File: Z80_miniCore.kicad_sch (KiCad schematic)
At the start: 40 parts, among them J1 ICSP, J2 UART, J3 I2C, J5 MicroSD, J7 USB_B_Mini, SW1 ON|OFF, SW2 Z80_RESET, SW3 CUSTOM, U1 Z84C00/PLCC, U2 PIC1-MMU, U3 28C256, U4 74HC138, U7 IS62C256AL, Y1 CANNED-DIP8, Y2 Crystal

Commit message: finish routing.
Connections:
- net GND: now also U4.5 (~{E1})
- net RFSH: no longer U4.5 (~{E1})
- no-connect marks 13 -> 14
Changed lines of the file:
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@@
+	)
+	(junction
+		(at 60.96 142.24)
+		(diameter 0)
+		(color 0 0 0 0)
 	)
 	(junction
@@
 	)
 	(no_connect
+		(at 22.86 41.91)
+	)
+	(no_connect
 		(at 245.11 115.57)
 	)
@@
 	(wire
 		(pts
+			(xy 60.96 142.24) (xy 60.96 149.86)
+		)
+		(stroke
+			(width 0)
+			(type default)
+		)
+	)
+	(wire
+		(pts
 			(xy 224.79 110.49) (xy 224.79 116.84)
 		)
@@
 	(wire
 		(pts
-			(xy 63.5 142.24) (xy 69.85 142.24)
+			(xy 60.96 142.24) (xy 69.85 142.24)
 		)
 		(stroke
@@
 	(wire
 		(pts
-			(xy 60.96 132.08) (xy 60.96 149.86)
+			(xy 60.96 132.08) (xy 60.96 142.24)
 		)
 		(stroke
@@
 		(effects
 			(font
-				(size 1.27 1.27)
-			)
-			(justify left bottom)
-		)
-	)
-	(label "RFSH"
-		(at 63.5 142.24 0)
-		(effects
-			(font

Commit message: Replace 8x10K_R w/ 1xRN8. Refine footprints.
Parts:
- removed R10, R11, R12, R4, R5, R6, R7, R9: 10K, Resistor_THT:R_Axial_DIN0207_L6.3mm_D2.5mm_P10.16mm_Horizontal, symbol Device:R
- added RN1: R_Network08, Resistor_THT:R_Array_SIP9, symbol Device:R_Network08
- C8: footprint Capacitor_THT:C_Disc_D3.4mm_W2.1mm_P2.50mm -> Capacitor_THT:C_Radial_D4.0mm_H5.0mm_P1.50mm
- C9: value 100uF -> 10uF
- J5: footprint Connector_PinSocket_2.54mm:PinSocket_1x06_P2.54mm_Vertical -> Connector_PinHeader_2.54mm:PinHeader_1x06_P2.54mm_Vertical
- R13: value 4k7 -> 10K
- R14: value 330 -> 10K
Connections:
- net BUSREQ: now also RN1.8 (R7)
- net INT: now also RN1.9 (R8)
- net IORQ: now also RN1.3 (R2)
- net MREQ: now also RN1.2 (R1)
- net NMI: now also RN1.7 (R6)
- net RD: now also RN1.4 (R3)
- net VCC: now also RN1.1 (common)
- net WAIT: now also RN1.6 (R5)
- net WR: now also RN1.5 (R4)

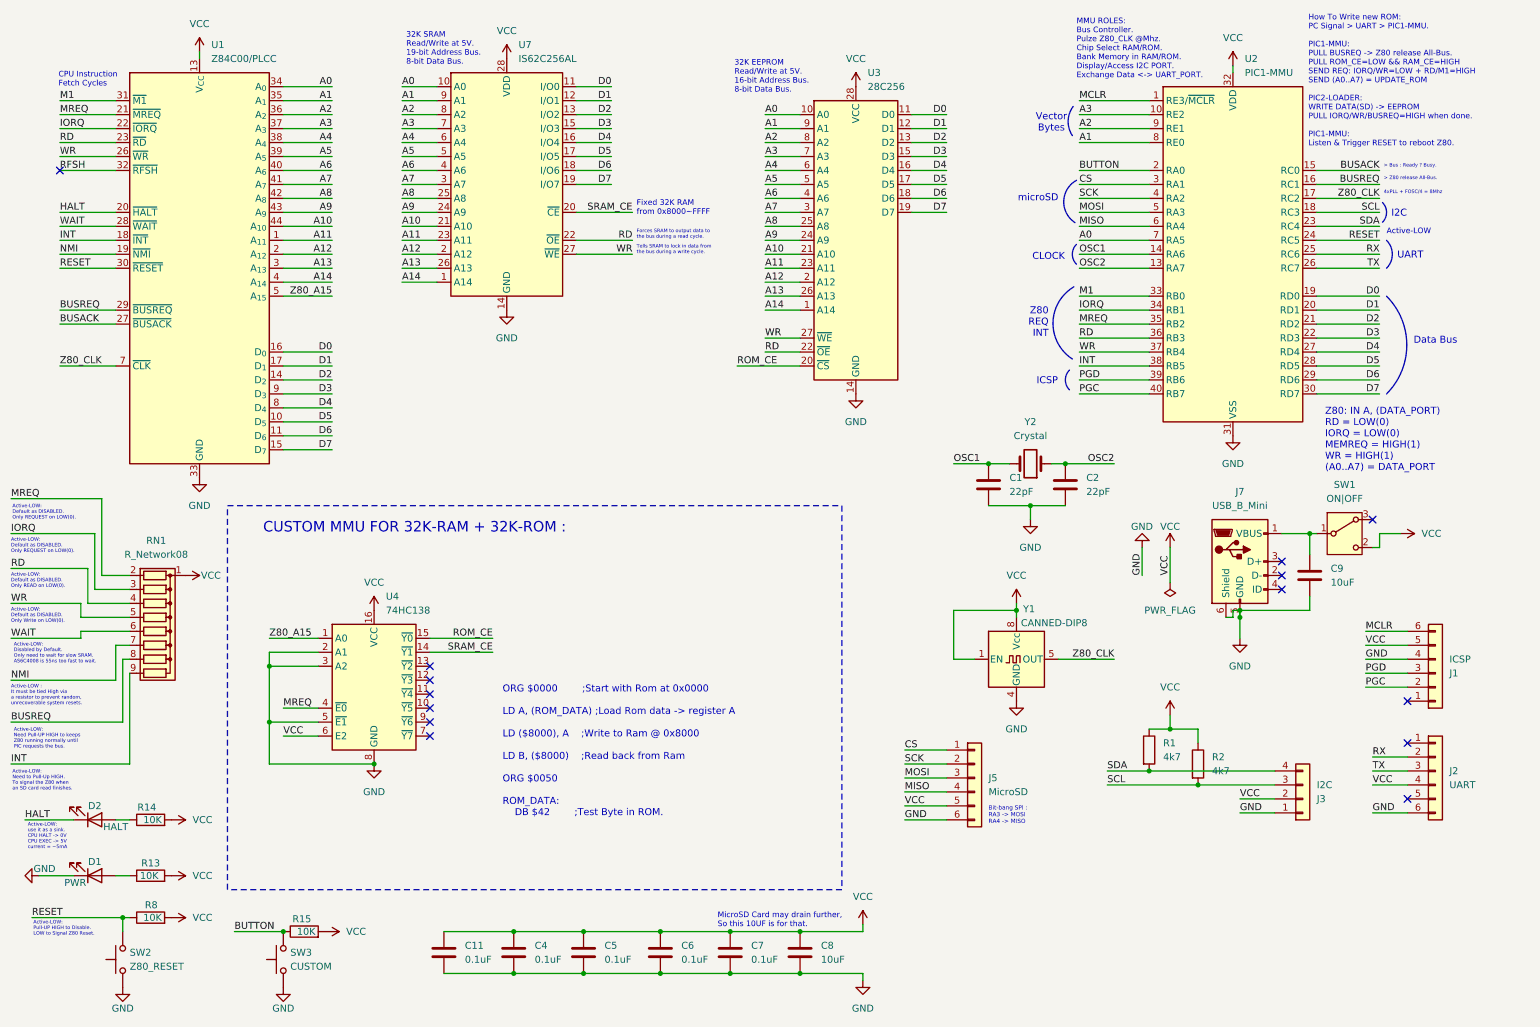
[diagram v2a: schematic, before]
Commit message: Refine schematic: convert all R-10K-> RN8 & fix ICSP.
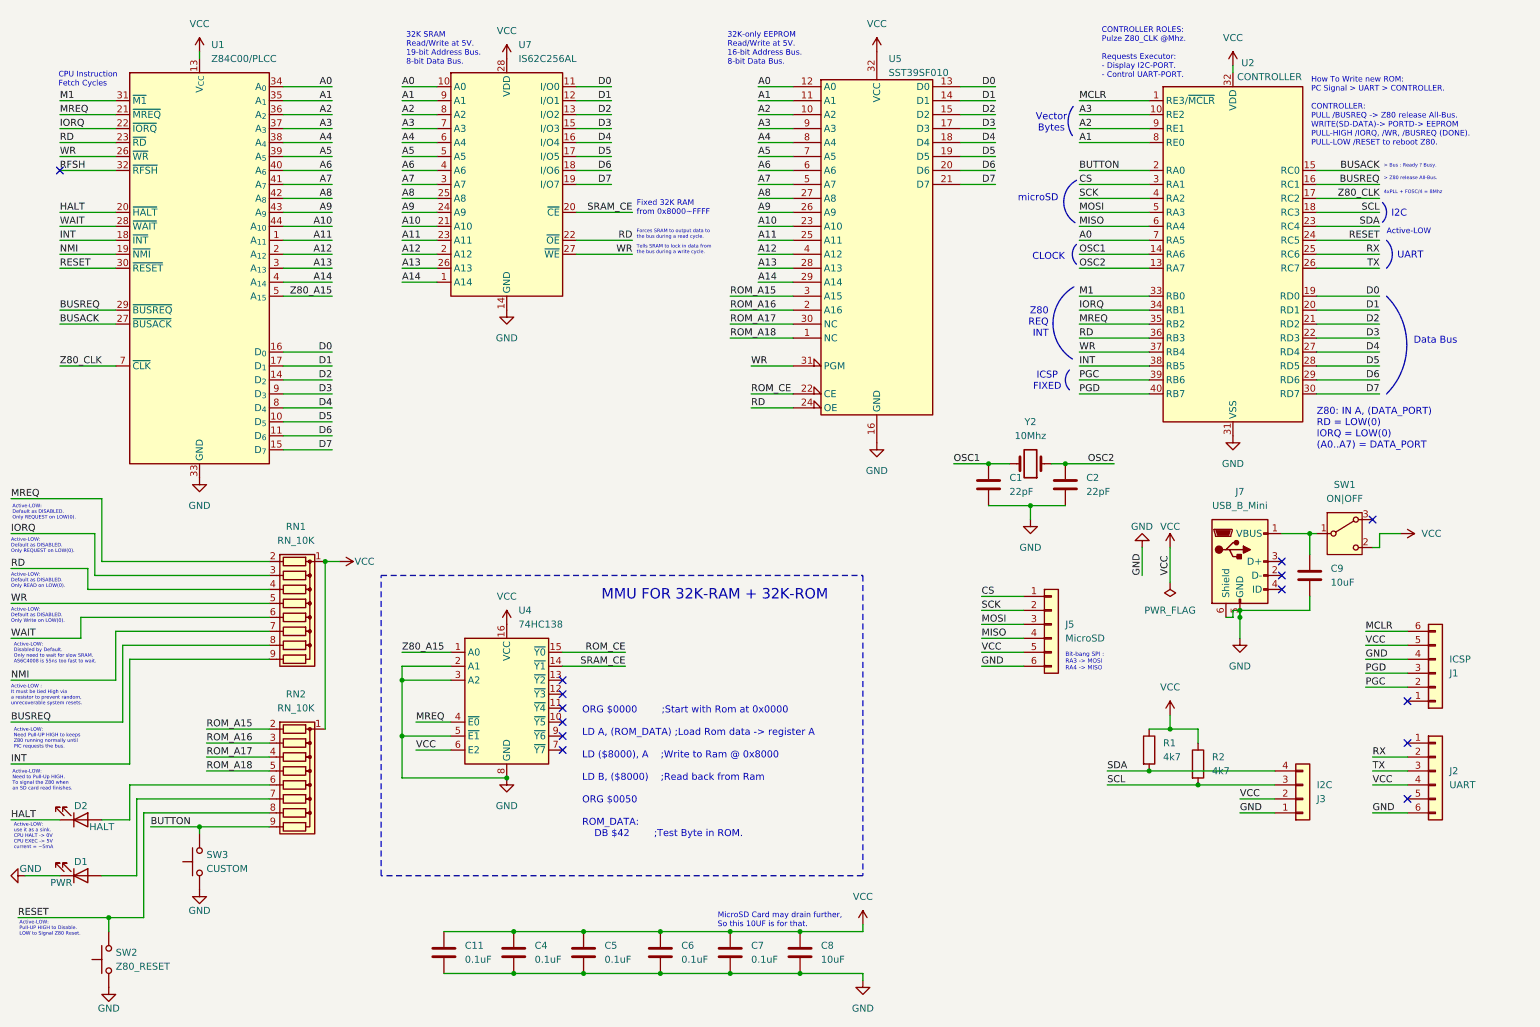
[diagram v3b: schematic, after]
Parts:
- removed R13, R14, R15, R8: 10K, Resistor_THT:R_Axial_DIN0207_L6.3mm_D2.5mm_P10.16mm_Horizontal, symbol Device:R
- removed U3: 28C256, Package_DIP:DIP-28_W15.24mm, symbol Memory_EEPROM:28C256
- removed Y1: CANNED-DIP8, Oscillator:Oscillator_DIP-8, symbol Oscillator:CXO_DIP8
- added RN2: RN_10K, Resistor_THT:R_Array_SIP9, symbol Device:R_Network08
- added U5: SST39SF010, Package_LCC:PLCC-32_THT-Socket, symbol Memory_Flash:SST39SF010
- RN1: value R_Network08 -> RN_10K
- U2: value PIC1-MMU -> CONTROLLER
- Y2: value Crystal -> 10Mhz
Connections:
- net A0: now also U5.12 (A0)
- net A1: now also U5.11 (A1)
- net A10: now also U5.23 (A10)
- net A11: now also U5.25 (A11)
- net A12: now also U5.4 (A12)
- net A13: now also U5.28 (A13)
- net A14: now also U5.29 (A14)
- net A2: now also U5.10 (A2)
- net A3: now also U5.9 (A3)
- net A4: now also U5.8 (A4)
- net A5: now also U5.7 (A5)
- net A6: now also U5.6 (A6)
- net A7: now also U5.5 (A7)
- net A8: now also U5.27 (A8)
- net A9: now also U5.26 (A9)
- net BUTTON: now also RN2.9 (R8)
- net D0: now also U5.13 (D0)
- net D1: now also U5.14 (D1)
- net D2: now also U5.15 (D2)
- net D3: now also U5.17 (D3)
- net D4: now also U5.18 (D4)
- net D5: now also U5.19 (D5)
- net D6: now also U5.20 (D6)
- net D7: now also U5.21 (D7)
- net GND: now also U5.16 (GND)
- net PGC: now also U2.39 (RB6); no longer U2.40 (RB7)
- net PGD: now also U2.40 (RB7); no longer U2.39 (RB6)
- net RD: now also U5.24 (OE)
- net RESET: now also RN2.8 (R7)
- net ROM_CE: now also U5.22 (CE)
- net VCC: now also RN2.1 (common), U5.32 (VCC)
- net WR: now also U5.31 (PGM)
- net at D1.2 (A): now also RN2.7 (R6)
- net at D2.2 (A): now also RN2.6 (R5)
- new net ROM_A15: RN2.2 (R1), U5.3 (A15)
- new net ROM_A16: RN2.3 (R2), U5.2 (A16)
- new net ROM_A17: RN2.4 (R3), U5.30 (NC)
- new net ROM_A18: RN2.5 (R4), U5.1 (NC)
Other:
- note added: "32K-only EEPROM Read/Write at 5V. 16-bit Address Bus. 8-bit Data Bus."
- note added: "CONTROLLER ROLES: Pulze Z80_CLK @Mhz. Requests Executor: - Display I2C-PORT. - Control UART-PORT."
- note added: "How To Write new ROM: PC Signal > UART > CONTROLLER. CONTROLLER: PULL /BUSREQ -> Z80 release All-Bus. WRITE(SD-DATA)-> PORTD-> EEPROM PULL-HIGH /IORQ, /WR, /BUSREQ (DONE). PULL-LOW /RESET to reboot Z80."
- note added: "ICSP FIXED"
- note added: "MMU FOR 32K-RAM + 32K-ROM"
- note added: "Z80: IN A, (DATA_PORT) RD = LOW(0) IORQ = LOW(0) (A0..A7) = DATA_PORT"
- note removed: "32K EEPROM Read/Write at 5V. 16-bit Address Bus. 8-bit Data Bus."
- note removed: "CUSTOM MMU FOR 32K-RAM + 32K-ROM :"
- note removed: "How To Write new ROM: PC Signal > UART > PIC1-MMU. PIC1-MMU: PULL BUSREQ -> Z80 release All-Bus. PULL ROM_CE=LOW && RAM_CE=HIGH SEND REQ: IORQ/WR=LOW + RD/M1=HIGH SEND (A0..A7) = UPDATE_ROM PIC2-LOADER: WRITE DATA(SD) -> EEPROM PULL IORQ/WR/BUSREQ=HIGH when done. PIC1-MMU: Listen & Trigger RESET to reboot Z80."
- note removed: "ICSP"
- note removed: "MMU ROLES: Bus Controller. Pulze Z80_CLK @Mhz. Chip Select RAM/ROM. Bank Memory in RAM/ROM. Display/Access I2C PORT. Exchange Data <-> UART_PORT."
- note removed: "Z80: IN A, (DATA_PORT) RD = LOW(0) IORQ = LOW(0) MEMREQ = HIGH(1) WR = HIGH(1) (A0..A7) = DATA_PORT"
- moved on the sheet: D1, D2, J5, RN1, SW2, SW3, U4
